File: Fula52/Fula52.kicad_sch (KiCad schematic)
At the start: 20 parts, among them J1 USB_C_Receptacle_USB2.0, U1 RT9013-33GB, U2 SRV05-4

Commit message: full routed
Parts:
- removed TP1, TP4: TestPoint, TestPoint:TestPoint_Pad_D2.5mm, symbol Connector:TestPoint
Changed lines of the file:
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@@
-    (pin "1")
-  )
-  (symbol (lib_id "power:GND") (at 252.73 60.96 0) (unit 1)
-    (in_bom yes) (on_board yes)
-    (property "Reference" "#PWR010" (id 0) (at 252.73 67.31 0)
-      (effects (font (size 1.27 1.27)) hide)
-    )
-    (property "Value" "GND" (id 1) (at 252.73 64.77 0))
-    (property "Footprint" "" (id 2) (at 252.73 60.96 0)
-      (effects (font (size 1.27 1.27)) hide)
-    )
-    (property "Datasheet" "" (id 3) (at 252.73 60.96 0)
-      (effects (font (size 1.27 1.27)) hide)
-    )
     (pin "1")
   )
@@
     )
     (property "Datasheet" "" (id 3) (at 134.62 69.85 0)
-      (effects (font (size 1.27 1.27)) hide)
-    )
-    (pin "1")
-  )
-  (symbol (lib_id "Connector:TestPoint") (at 236.22 50.8 270) (unit 1)
-    (in_bom no) (on_board yes)
-    (property "Reference" "TP1" (id 0) (at 242.57 50.8 90))
-    (property "Value" "TestPoint" (id 1) (at 245.11 49.53 90)
-      (effects (font (size 1.27 1.27)) hide)
-    )
-    (property "Footprint" "TestPoint:TestPoint_Pad_D2.5mm" (id 2) (at 236.22 55.88 0)
-      (effects (font (size 1.27 1.27)) hide)
-    )
-    (property "Datasheet" "~" (id 3) (at 236.22 55.88 0)
       (effects (font (size 1.27 1.27)) hide)
     )
@@
     (pin "1")
   )
-  (symbol (lib_id "Connector:TestPoint") (at 252.73 60.96 0) (unit 1)
-    (in_bom no) (on_board yes)
-    (property "Reference" "TP4" (id 0) (at 252.73 55.88 0))
-    (property "Value" "TestPoint" (id 1) (at 251.46 52.07 90)
-      (effects (font (size 1.27 1.27)) hide)
-    )
-    (property "Footprint" "TestPoint:TestPoint_Pad_D2.5mm" (id 2) (at 257.81 60.96 0)
-      (effects (font (size 1.27 1.27)) hide)
-    )
-    (property "Datasheet" "~" (id 3) (at 257.81 60.96 0)
-      (effects (font (size 1.27 1.27)) hide)
-    )
-    (pin "1")
-  )
   (symbol (lib_id "Device:R") (at 67.31 43.18 90) (unit 1)
     (in_bom yes) (on_board yes)
@@
       (reference "#PWR09") (unit 1) (value "GND") (footprint "")
     )
-    (path "/2a64dcda-edcc-40e4-8e7c-d368b6df665f"
-      (reference "#PWR010") (unit 1) (value "GND") (footprint "")
-    )
     (path "/40cc8c50-15d7-4d1f-befc-4c0a9cc13eb3"
       (reference "#PWR011") (unit 1) (value "GND") (footprint "")
@@
       (reference "SW2") (unit 1) (value "RESET") (footprint "Button_Switch_SMD:SW_SPST_CK_RS282G05A3")
     )
-    (path "/4d64b221-2006-4be2-8f3e-495e244ba60d"
-      (reference "TP1") (unit 1) (value "TestPoint") (footprint "TestPoint:TestPoint_Pad_D2.5mm")
-    )
     (path "/09e661ab-7055-44f5-a412-31ad25f12e9b"
       (reference "TP2") (unit 1) (value "TestPoint") (footprint "TestPoint:TestPoint_Pad_1.5x1.5mm")
@@
       (reference "TP3") (unit 1) (value "TestPoint") (footprint "TestPoint:TestPoint_Pad_1.5x1.5mm")
     )
-    (path "/dcdee9f3-7399-4d27-a1b1-8fda0194cb65"
-      (reference "TP4") (unit 1) (value "TestPoint") (footprint "TestPoint:TestPoint_Pad_D2.5mm")
-    )
     (path "/cf5ee326-e078-4bf6-ba2d-41e060b62395"

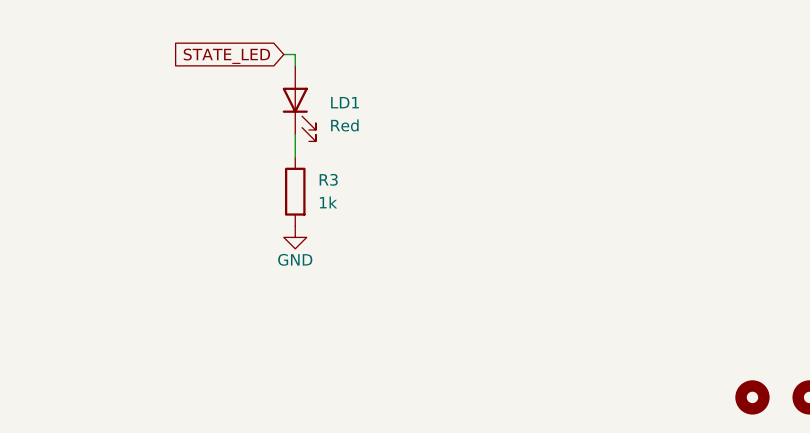
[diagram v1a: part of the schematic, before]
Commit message: Rename, from Fula52 to Calcite52
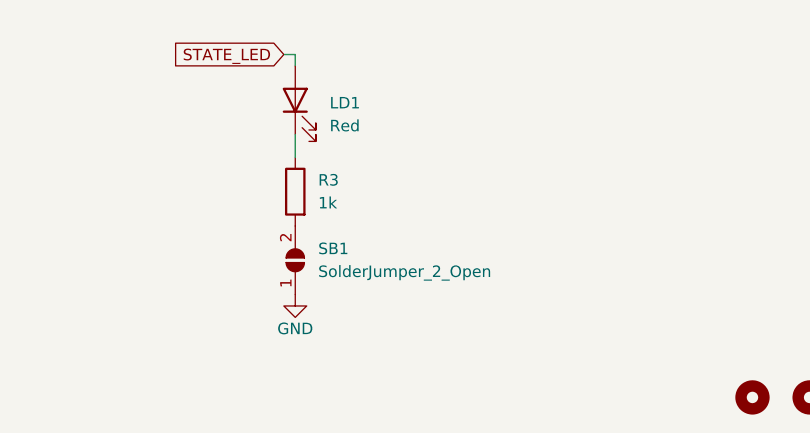
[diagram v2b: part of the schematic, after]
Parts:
- added SB1: SolderJumper_2_Open, Jumper:SolderJumper-2_P1.3mm_Open_TrianglePad1.0x1.5mm, symbol Jumper:SolderJumper_2_Open
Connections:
- net GND: now also SB1.1 (A); no longer R3.2
- new net: R3.2, SB1.2 (B)
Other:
- title: Fula52 Keyboard -> Calcite52 Keyboard
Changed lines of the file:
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@@
   (paper "A4")
   (title_block
-    (title "Fula52 Keyboard")
+    (title "Calcite52 Keyboard")
     (rev "1.0")
     (comment 1 "MIT License (Open source hardware)")
@@
       (effects (font (size 1.27 1.27)) hide)
     )
+  )
+  (symbol (lib_id "Jumper:SolderJumper_2_Open") (at 91.44 179.07 90) (unit 1)
+    (in_bom yes) (on_board yes) (fields_autoplaced)
+    (property "Reference" "SB1" (id 0) (at 93.98 177.7999 90)
+      (effects (font (size 1.27 1.27)) (justify right))
+    )
+    (property "Value" "SolderJumper_2_Open" (id 1) (at 93.98 180.3399 90)
+      (effects (font (size 1.27 1.27)) (justify right))
+    )
+    (property "Footprint" "Jumper:SolderJumper-2_P1.3mm_Open_TrianglePad1.0x1.5mm" (id 2) (at 91.44 179.07 0)
+      (effects (font (size 1.27 1.27)) hide)
+    )
+    (property "Datasheet" "~" (id 3) (at 91.44 179.07 0)
+      (effects (font (size 1.27 1.27)) hide)
+    )
+    (pin "1")
+    (pin "2")
   )
   (symbol (lib_id "Device:LED") (at 91.44 161.29 90) (unit 1)
@@
     (pin "1")
   )
-  (symbol (lib_id "power:GND") (at 91.44 175.26 0) (unit 1)
-    (in_bom yes) (on_board yes)
-    (property "Reference" "#PWR0101" (id 0) (at 91.44 181.61 0)
-      (effects (font (size 1.27 1.27)) hide)
-    )
-    (property "Value" "GND" (id 1) (at 91.44 179.07 0))
-    (property "Footprint" "" (id 2) (at 91.44 175.26 0)
-      (effects (font (size 1.27 1.27)) hide)
-    )
-    (property "Datasheet" "" (id 3) (at 91.44 175.26 0)
+  (symbol (lib_id "power:GND") (at 91.44 182.88 0) (unit 1)
+    (in_bom yes) (on_board yes)
+    (property "Reference" "#PWR0101" (id 0) (at 91.44 189.23 0)
+      (effects (font (size 1.27 1.27)) hide)
+    )
+    (property "Value" "GND" (id 1) (at 91.44 186.69 0))
+    (property "Footprint" "" (id 2) (at 91.44 182.88 0)
+      (effects (font (size 1.27 1.27)) hide)
+    )
+    (property "Datasheet" "" (id 3) (at 91.44 182.88 0)
       (effects (font (size 1.27 1.27)) hide)
     )
@@
       (reference "R9") (unit 1) (value "10k") (footprint "Resistor_SMD:R_0402_1005Metric")
     )
+    (path "/59187f40-b3d9-425d-9e55-e25fe1fb020b"
+      (reference "SB1") (unit 1) (value "SolderJumper_2_Open") (footprint "Jumper:SolderJumper-2_P1.3mm_Open_TrianglePad1.0x1.5mm")
+    )
     (path "/946b7d05-a76d-4dab-8c7f-ee314175ff48/408f5b7a-60d9-4b4f-994c-d2f20e67a312"
